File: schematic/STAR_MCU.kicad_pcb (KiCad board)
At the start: 2 copper layers, 39 parts, among them J1 HC-SR04, J11 6120XX21621_61200621621, J13 6120XX21621_61200821621, J14 6120XX21621_61200821621, J15 6120XX21621_61200821621, J16 6120XX21621_61200821621, J17 USB4216-03-A, J18 6120XX21621_61200621621, J19 6120XX21621_61200821621, J2 HC-SR04, J20 S5B-XH-A, J21 6120XX21621_61200621621, J3 HC-SR04, J4 HC-SR04, J5 HC-SR04, J6 HC-SR04, J8 Conn_02x20_Odd_Even, U1 DS18B20+, U2 ESP32-S3-WROOM-1-N16, U3 74HC139D,653, U4 SN74HC153DR, U5 RP2350_Stamp_XL

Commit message: Normalize KiCad symbol library structure
- Remove ul_ prefixes from Ultra Librarian exports (10 directories renamed, 2 duplicates deleted)
- Flatten directory structure (remove KiCad/KiCADv6 subdirectories from 93 components)
- Replace date-stamped filenames with part numbers (3 files renamed)
- Standardize separators: comma to hyphen (7 directories renamed)
- Update library table references (sym-lib-table: 84 entries, fp-lib-table: 85 entries)
- Update all schematic and PCB references (10 schematics + 10 PCBs)

Total changes:
- 100 component directories normalized to flat structure
- All library references updated and validated
- No ul_ prefixes, KiCad subdirs, date-stamped files, or commas in names remain
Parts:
- U3, U4: footprint 74HC139D,653:SOIC127P600X175-16N -> 74HC139D-653:SOIC127P600X175-16N
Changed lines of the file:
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@@
 		(embedded_fonts no)
 	)
-	(footprint "74HC139D,653:SOIC127P600X175-16N"
+	(footprint "74HC139D-653:SOIC127P600X175-16N"
 		(layer "F.Cu")
 		(at 152.18 123.2)
@@
 		)
 	)
-	(footprint "74HC139D,653:SOIC127P600X175-16N"
+	(footprint "74HC139D-653:SOIC127P600X175-16N"
 		(layer "F.Cu")
 		(at 143.63 123.2)

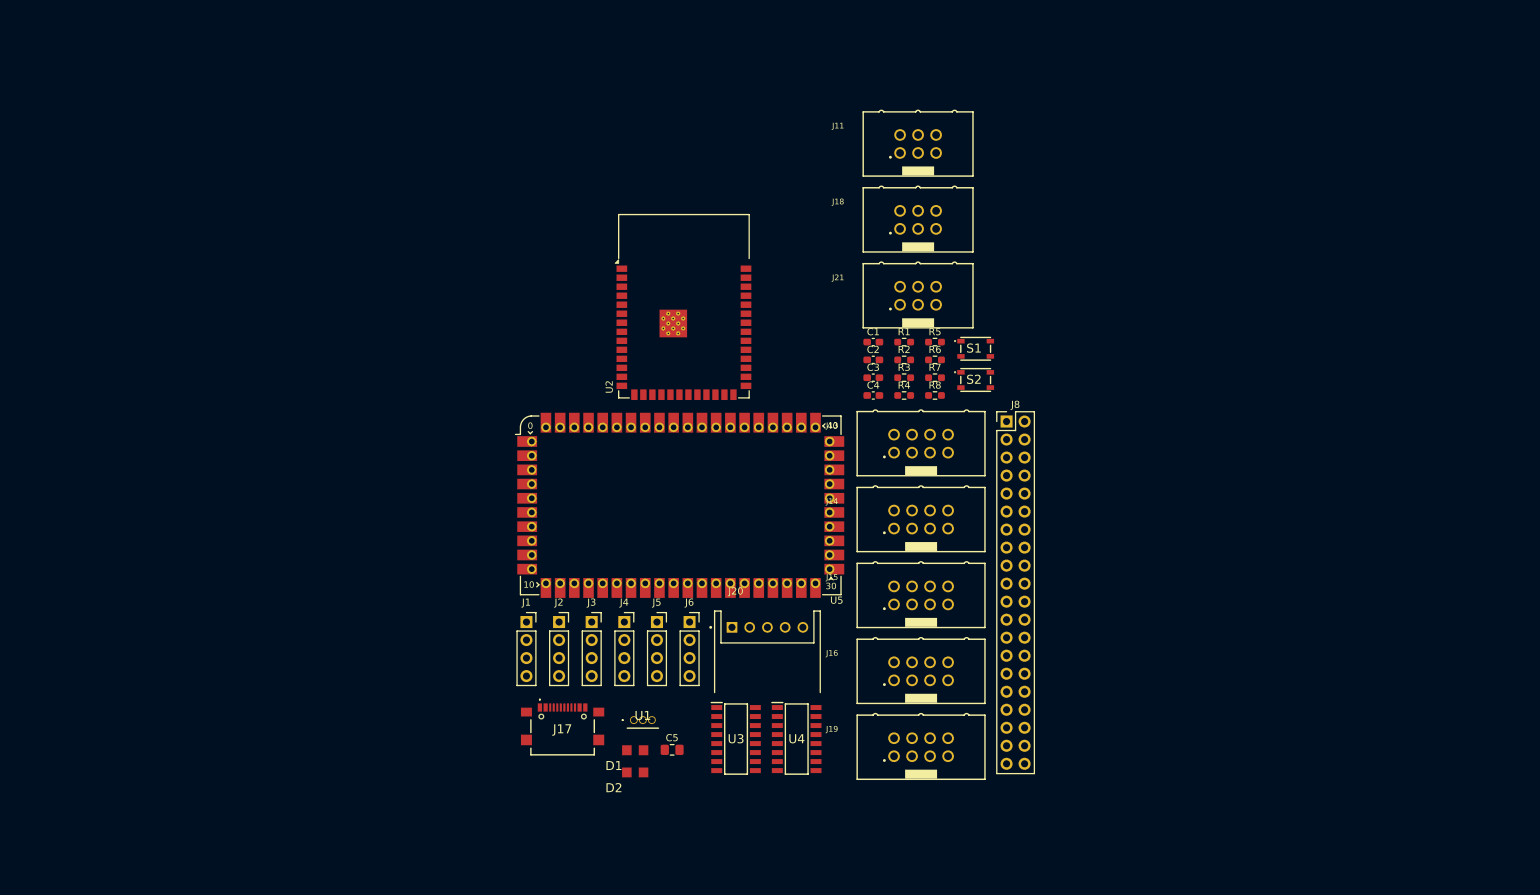
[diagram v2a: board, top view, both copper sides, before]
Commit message: fixed usb-c
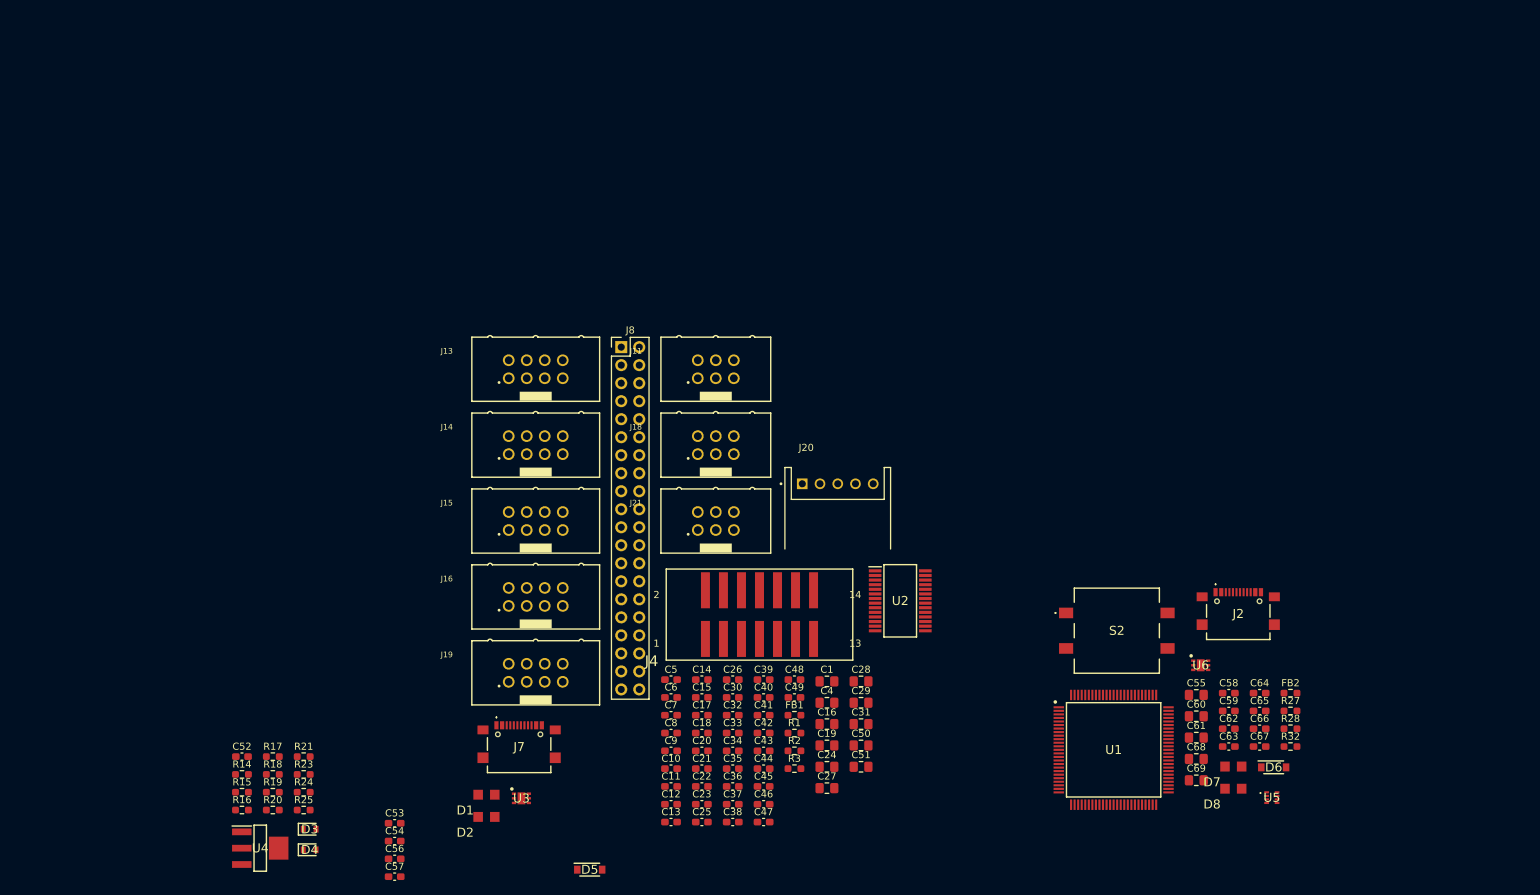
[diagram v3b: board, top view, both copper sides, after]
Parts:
- removed C2: 1u, Capacitor_SMD:C_0603_1608Metric_Pad1.08x0.95mm_HandSolder
- removed C3: 100n, Capacitor_SMD:C_0603_1608Metric_Pad1.08x0.95mm_HandSolder
- removed J1, J3, J5, J6: HC-SR04, Connector_PinSocket_2.54mm:PinSocket_1x04_P2.54mm_Vertical
- removed J17: USB4216-03-A, USB4216-03-A:USB421603A
- removed R4, R5, R8: 10k, Resistor_SMD:R_0603_1608Metric_Pad0.98x0.95mm_HandSolder
- removed R6, R7: 5k1, Resistor_SMD:R_0603_1608Metric_Pad0.98x0.95mm_HandSolder
- removed S1: ESP_RST, SKRPACE010:SMT_4.2X3.2_
- added C10: 1u, Capacitor_SMD:C_0603_1608Metric_Pad1.08x0.95mm_HandSolder, F.Cu at (134.5, 127.4)
- added C11: 1u, Capacitor_SMD:C_0603_1608Metric_Pad1.08x0.95mm_HandSolder, F.Cu at (134.5, 129.9)
- added C12: 1u, Capacitor_SMD:C_0603_1608Metric_Pad1.08x0.95mm_HandSolder, F.Cu at (134.5, 132.4)
- added C13: 1u, Capacitor_SMD:C_0603_1608Metric_Pad1.08x0.95mm_HandSolder, F.Cu at (134.5, 134.9)
- added C14: 1u, Capacitor_SMD:C_0603_1608Metric_Pad1.08x0.95mm_HandSolder, F.Cu at (138.8, 114.8)
- added C15: 220n, Capacitor_SMD:C_0603_1608Metric_Pad1.08x0.95mm_HandSolder, F.Cu at (138.8, 117.3)
- added C16: 10u, Capacitor_SMD:C_0805_2012Metric_Pad1.18x1.45mm_HandSolder, F.Cu at (156.4, 121.1)
- added C17: 100n, Capacitor_SMD:C_0603_1608Metric_Pad1.08x0.95mm_HandSolder, F.Cu at (138.8, 119.8)
- added C18: 10n, Capacitor_SMD:C_0603_1608Metric_Pad1.08x0.95mm_HandSolder, F.Cu at (138.8, 122.3)
- added C19: 10u, Capacitor_SMD:C_0805_2012Metric_Pad1.18x1.45mm_HandSolder, F.Cu at (156.4, 124.1)
- added C20: 100n, Capacitor_SMD:C_0603_1608Metric_Pad1.08x0.95mm_HandSolder, F.Cu at (138.8, 124.9)
- added C21: 1u, Capacitor_SMD:C_0603_1608Metric_Pad1.08x0.95mm_HandSolder, F.Cu at (138.8, 127.4)
- added C22: 1u, Capacitor_SMD:C_0603_1608Metric_Pad1.08x0.95mm_HandSolder, F.Cu at (138.8, 129.9)
- added C23: 10n, Capacitor_SMD:C_0603_1608Metric_Pad1.08x0.95mm_HandSolder, F.Cu at (138.8, 132.4)
- added C24: 10u, Capacitor_SMD:C_0805_2012Metric_Pad1.18x1.45mm_HandSolder, F.Cu at (156.4, 127.1)
- added C25: 100n, Capacitor_SMD:C_0603_1608Metric_Pad1.08x0.95mm_HandSolder, F.Cu at (138.8, 134.9)
- added C26: 10n, Capacitor_SMD:C_0603_1608Metric_Pad1.08x0.95mm_HandSolder, F.Cu at (143.2, 114.8)
- added C27: 10u, Capacitor_SMD:C_0805_2012Metric_Pad1.18x1.45mm_HandSolder, F.Cu at (156.4, 130.1)
- added C28: 10u, Capacitor_SMD:C_0805_2012Metric_Pad1.18x1.45mm_HandSolder, F.Cu at (161.3, 115.1)
- added C29: 10u, Capacitor_SMD:C_0805_2012Metric_Pad1.18x1.45mm_HandSolder, F.Cu at (161.3, 118.1)
- added C30: 100n, Capacitor_SMD:C_0603_1608Metric_Pad1.08x0.95mm_HandSolder, F.Cu at (143.2, 117.3)
- added C31: 10u, Capacitor_SMD:C_0805_2012Metric_Pad1.18x1.45mm_HandSolder, F.Cu at (161.3, 121.1)
- added C32: 10n, Capacitor_SMD:C_0603_1608Metric_Pad1.08x0.95mm_HandSolder, F.Cu at (143.2, 119.8)
- added C33: 100n, Capacitor_SMD:C_0603_1608Metric_Pad1.08x0.95mm_HandSolder, F.Cu at (143.2, 122.3)
- added C34: 100n, Capacitor_SMD:C_0603_1608Metric_Pad1.08x0.95mm_HandSolder, F.Cu at (143.2, 124.9)
- added C35: 100n, Capacitor_SMD:C_0603_1608Metric_Pad1.08x0.95mm_HandSolder, F.Cu at (143.2, 127.4)
- added C36: 100n, Capacitor_SMD:C_0603_1608Metric_Pad1.08x0.95mm_HandSolder, F.Cu at (143.2, 129.9)
- added C37: 100n, Capacitor_SMD:C_0603_1608Metric_Pad1.08x0.95mm_HandSolder, F.Cu at (143.2, 132.4)
- added C38: 100n, Capacitor_SMD:C_0603_1608Metric_Pad1.08x0.95mm_HandSolder, F.Cu at (143.2, 134.9)
- added C39: 100n, Capacitor_SMD:C_0603_1608Metric_Pad1.08x0.95mm_HandSolder, F.Cu at (147.5, 114.8)
- added C40: 100n, Capacitor_SMD:C_0603_1608Metric_Pad1.08x0.95mm_HandSolder, F.Cu at (147.5, 117.3)
- added C41: 100n, Capacitor_SMD:C_0603_1608Metric_Pad1.08x0.95mm_HandSolder, F.Cu at (147.5, 119.8)
- added C42: 100n, Capacitor_SMD:C_0603_1608Metric_Pad1.08x0.95mm_HandSolder, F.Cu at (147.5, 122.3)
- added C43: 1u, Capacitor_SMD:C_0603_1608Metric_Pad1.08x0.95mm_HandSolder, F.Cu at (147.5, 124.9)
- added C44: 100n, Capacitor_SMD:C_0603_1608Metric_Pad1.08x0.95mm_HandSolder, F.Cu at (147.5, 127.4)
- added C45: 10n, Capacitor_SMD:C_0603_1608Metric_Pad1.08x0.95mm_HandSolder, F.Cu at (147.5, 129.9)
- added C46: 10n, Capacitor_SMD:C_0603_1608Metric_Pad1.08x0.95mm_HandSolder, F.Cu at (147.5, 132.4)
- added C47: 10n, Capacitor_SMD:C_0603_1608Metric_Pad1.08x0.95mm_HandSolder, F.Cu at (147.5, 134.9)
- added C48: 10n, Capacitor_SMD:C_0603_1608Metric_Pad1.08x0.95mm_HandSolder, F.Cu at (151.9, 114.8)
- added C49: 100n, Capacitor_SMD:C_0603_1608Metric_Pad1.08x0.95mm_HandSolder, F.Cu at (151.9, 117.3)
- added C50: 4u7, Capacitor_SMD:C_0805_2012Metric_Pad1.18x1.45mm_HandSolder, F.Cu at (161.3, 124.1)
- added C51: 4u7, Capacitor_SMD:C_0805_2012Metric_Pad1.18x1.45mm_HandSolder, F.Cu at (161.3, 127.1)
- added C52: 1u, Capacitor_SMD:C_0603_1608Metric_Pad1.08x0.95mm_HandSolder, F.Cu at (74.0, 125.7)
- added C53: 1u, Capacitor_SMD:C_0603_1608Metric_Pad1.08x0.95mm_HandSolder, F.Cu at (95.5, 135.1)
- added C54: 100n, Capacitor_SMD:C_0603_1608Metric_Pad1.08x0.95mm_HandSolder, F.Cu at (95.5, 137.6)
- added C55: 4u7, Capacitor_SMD:C_0805_2012Metric_Pad1.18x1.45mm_HandSolder, F.Cu at (208.5, 117.0)
- added C56: 1u, Capacitor_SMD:C_0603_1608Metric_Pad1.08x0.95mm_HandSolder, F.Cu at (95.5, 140.1)
- added C57: 100n, Capacitor_SMD:C_0603_1608Metric_Pad1.08x0.95mm_HandSolder, F.Cu at (95.5, 142.6)
- added C58: 1u, Capacitor_SMD:C_0603_1608Metric_Pad1.08x0.95mm_HandSolder, F.Cu at (213.1, 116.7)
- added C59: 1u, Capacitor_SMD:C_0603_1608Metric_Pad1.08x0.95mm_HandSolder, F.Cu at (213.1, 119.2)
- added C6: 1u, Capacitor_SMD:C_0603_1608Metric_Pad1.08x0.95mm_HandSolder, F.Cu at (134.5, 117.3)
- added C60: 10u, Capacitor_SMD:C_0805_2012Metric_Pad1.18x1.45mm_HandSolder, F.Cu at (208.5, 120.0)
- added C61: 10u, Capacitor_SMD:C_0805_2012Metric_Pad1.18x1.45mm_HandSolder, F.Cu at (208.5, 123.0)
- added C62: 1u, Capacitor_SMD:C_0603_1608Metric_Pad1.08x0.95mm_HandSolder, F.Cu at (213.1, 121.7)
- added C63: 10n, Capacitor_SMD:C_0603_1608Metric_Pad1.08x0.95mm_HandSolder, F.Cu at (213.1, 124.3)
- added C64: 10n, Capacitor_SMD:C_0603_1608Metric_Pad1.08x0.95mm_HandSolder, F.Cu at (217.4, 116.7)
- added C65: 10n, Capacitor_SMD:C_0603_1608Metric_Pad1.08x0.95mm_HandSolder, F.Cu at (217.4, 119.2)
- added C66: 10n, Capacitor_SMD:C_0603_1608Metric_Pad1.08x0.95mm_HandSolder, F.Cu at (217.4, 121.7)
- added C67: 100n, Capacitor_SMD:C_0603_1608Metric_Pad1.08x0.95mm_HandSolder, F.Cu at (217.4, 124.3)
- added C68: 4u7, Capacitor_SMD:C_0805_2012Metric_Pad1.18x1.45mm_HandSolder, F.Cu at (208.5, 126.0)
- added C69: 4u7, Capacitor_SMD:C_0805_2012Metric_Pad1.18x1.45mm_HandSolder, F.Cu at (208.5, 129.0)
- added C7: 1u, Capacitor_SMD:C_0603_1608Metric_Pad1.08x0.95mm_HandSolder, F.Cu at (134.5, 119.8)
- added C8: 1u, Capacitor_SMD:C_0603_1608Metric_Pad1.08x0.95mm_HandSolder, F.Cu at (134.5, 122.3)
- added C9: 1u, Capacitor_SMD:C_0603_1608Metric_Pad1.08x0.95mm_HandSolder, F.Cu at (134.5, 124.9)
- added D3: RED, SML-D12Y1WT86:LEDC1608X55N, F.Cu at (83.5, 135.9)
- added D4: RED, SML-D12Y1WT86:LEDC1608X55N, F.Cu at (83.5, 138.8)
- added D5: 1N4007W-T, 1N4007W-T:SODFL3818X130N, F.Cu at (123.0, 141.6)
- added D6: 1N4007W-T, 1N4007W-T:SODFL3818X130N, F.Cu at (219.4, 127.2)
- added D7: 82306050029, 82306050029:WESURGE_0603134, F.Cu at (213.7, 127.1)
- added D8: 82306050029, 82306050029:WESURGE_0603134, F.Cu at (213.7, 130.2)
- added FB1: 22R, Resistor_SMD:R_0603_1608Metric_Pad0.98x0.95mm_HandSolder, F.Cu at (151.9, 119.8)
- added FB2: 22R, Resistor_SMD:R_0603_1608Metric_Pad0.98x0.95mm_HandSolder, F.Cu at (221.8, 116.7)
- added J7: USB4216-03-A, USB4216-03-A:USB421603A, F.Cu at (113.0, 124.6)
- added R14: 1k, Resistor_SMD:R_0603_1608Metric_Pad0.98x0.95mm_HandSolder, F.Cu at (74.0, 128.2)
- added R15: 1k, Resistor_SMD:R_0603_1608Metric_Pad0.98x0.95mm_HandSolder, F.Cu at (74.0, 130.7)
- added R16: 10k, Resistor_SMD:R_0603_1608Metric_Pad0.98x0.95mm_HandSolder, F.Cu at (74.0, 133.2)
- added R17: 10k, Resistor_SMD:R_0603_1608Metric_Pad0.98x0.95mm_HandSolder, F.Cu at (78.3, 125.7)
- added R18: 10k, Resistor_SMD:R_0603_1608Metric_Pad0.98x0.95mm_HandSolder, F.Cu at (78.3, 128.2)
- added R19: 10k, Resistor_SMD:R_0603_1608Metric_Pad0.98x0.95mm_HandSolder, F.Cu at (78.3, 130.7)
- added R20: 10k, Resistor_SMD:R_0603_1608Metric_Pad0.98x0.95mm_HandSolder, F.Cu at (78.3, 133.2)
- added R21: 10k, Resistor_SMD:R_0603_1608Metric_Pad0.98x0.95mm_HandSolder, F.Cu at (82.7, 125.7)
- added R23: 10k, Resistor_SMD:R_0603_1608Metric_Pad0.98x0.95mm_HandSolder, F.Cu at (82.7, 128.2)
- added R24: 10k, Resistor_SMD:R_0603_1608Metric_Pad0.98x0.95mm_HandSolder, F.Cu at (82.7, 130.7)
- added R25: 10k, Resistor_SMD:R_0603_1608Metric_Pad0.98x0.95mm_HandSolder, F.Cu at (82.7, 133.2)
- added R27: 10k, Resistor_SMD:R_0603_1608Metric_Pad0.98x0.95mm_HandSolder, F.Cu at (221.8, 119.2)
- added R28: 10k, Resistor_SMD:R_0603_1608Metric_Pad0.98x0.95mm_HandSolder, F.Cu at (221.8, 121.7)
- added R32: 15k, Resistor_SMD:R_0603_1608Metric_Pad0.98x0.95mm_HandSolder, F.Cu at (221.8, 124.3)
- added U6: TVS2200DRV, TVS2200DRVR:SON65P200X200X80-7N, F.Cu at (209.1, 112.8)
- C1, C4: value 100n -> 10u; footprint Capacitor_SMD:C_0603_1608Metric_Pad1.08x0.95mm_HandSolder -> Capacitor_SMD:C_0805_2012Metric_Pad1.18x1.45mm_HandSolder
- C5: value 10u -> 100n; footprint Capacitor_SMD:C_0805_2012Metric_Pad1.18x1.45mm_HandSolder -> Capacitor_SMD:C_0603_1608Metric_Pad1.08x0.95mm_HandSolder
- J2: value HC-SR04 -> USB4216-03-A; footprint Connector_PinSocket_2.54mm:PinSocket_1x04_P2.54mm_Vertical -> USB4216-03-A:USB421603A
- J4: value HC-SR04 -> E1E2-Emulator-Interface; footprint Connector_PinSocket_2.54mm:PinSocket_1x04_P2.54mm_Vertical -> E1E2-Emulator-Interface:SAMTEC-HTST-107-01-X-DV
- S2: value ESP_BOOT -> PTS125SM73SMTR21M_LFS; footprint SKRPACE010:SMT_4.2X3.2_ -> PTS125SM73SMTR21M_LFS:PTS125SM73SMTR21MLFS
- U1: value DS18B20+ -> R5F572NNHGFP-30; footprint DS18B20+:DS18B20 -> R5F572NNHGFP-30:QFP50P1600X1600X170-100N
- U2: value ESP32-S3-WROOM-1-N16 -> CY7C65213A-28PVXI; footprint RF_Module:ESP32-S3-WROOM-1 -> CY7C65213A-28PVXI:SOP65P780X200-28N
- U3: value 74HC139D,653 -> TVS2200DRV; footprint 74HC139D-653:SOIC127P600X175-16N -> TVS2200DRVR:SON65P200X200X80-7N
- U4: value SN74HC153DR -> LDL1117S33R; footprint 74HC139D-653:SOIC127P600X175-16N -> LDL1117S33R:SOT230P700X180-4N
- U5: value RP2350_Stamp_XL -> TPS2116DRLR; footprint rp2xxx:RP2xxx_Stamp_XL_THT -> TPS2116DRLR:TPS62932DRLR
- moved J2 95.8 mm to (214.4, 105.8)
- moved U5 93.0 mm to (219.2, 131.5)
- moved U4 77.2 mm to (76.5, 138.6)
- moved U1 66.5 mm to (196.9, 124.7)
- moved R2 57.2 mm to (151.9, 124.9)
- moved R3 57.2 mm to (151.9, 127.4)
- moved R1 57.2 mm to (151.9, 122.3)
- moved J8 55.3 mm to (127.4, 67.9)
- moved J13 55.3 mm to (115.4, 71.1)
- moved J14 55.3 mm to (115.4, 81.8)
- moved J15 55.3 mm to (115.4, 92.5)
- moved J16 55.3 mm to (115.4, 103.2)
- moved J19 55.3 mm to (115.4, 113.9)
- moved U2 51.5 mm to (166.8, 103.7)
- moved C1 48.3 mm to (156.4, 115.1)
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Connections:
- C1 pad 1: GND -> /BOARD_3V3
- C1 pad 2: Net-(C1-Pad2) -> GND
- C4 pad 1: GND -> /BOARD_3V3
- C4 pad 2: /MOTOR_DRIVER_P3V3 -> AVSS0-1
- C5 pad 1: /MOTOR_DRIVER_P3V3 -> /BOARD_3V3
- D1 pad 1: /USB_C_P -> /SCI_USBC_USBDP
- D2 pad 1: /USB_C_N -> /SCI_USBC_USBDN
- J4 pad 1: /MOTOR_DRIVER_P3V3 -> /EMU_TCK
- J4 pad 2: /HCSR04_TRIG4 -> GND
- J4 pad 3: /HCSR04_ECHO4 -> /EMU_TRSTn
- J4 pad 4: GND -> /EMU_EMLE
- J8 pad 11: /HCSR04_ECHO1 -> unconnected-(J8-Pin_11-Pad11)
- J8 pad 12: /HCSR04_TRIG4 -> unconnected-(J8-Pin_12-Pad12)
- J8 pad 13: /HCSR04_TRIG2 -> unconnected-(J8-Pin_13-Pad13)
- J8 pad 15: /HCSR04_ECHO2 -> unconnected-(J8-Pin_15-Pad15)
- J8 pad 22: /HCSR04_ECHO4 -> unconnected-(J8-Pin_22-Pad22)
- J8 pad 26: /HCSR04_TRIG5 -> unconnected-(J8-Pin_26-Pad26)
- J8 pad 27: /MOTOR_DRIVER_MOTOR4_nFAULT -> unconnected-(J8-Pin_27-Pad27)
- J8 pad 28: /HCSR04_ECHO5 -> unconnected-(J8-Pin_28-Pad28)
- J8 pad 29: /MOTOR_DRIVER_MOTOR3_nFAULT -> unconnected-(J8-Pin_29-Pad29)
- J8 pad 31: /MOTOR_DRIVER_MOTOR2_nFAULT -> unconnected-(J8-Pin_31-Pad31)
- J8 pad 32: /HCSR04_TRIG6 -> unconnected-(J8-Pin_32-Pad32)
- J8 pad 33: /MOTOR_DRIVER_MOTOR1_nFAULT -> unconnected-(J8-Pin_33-Pad33)
- J8 pad 35: /HCSR04_TRIG3 -> unconnected-(J8-Pin_35-Pad35)
- J8 pad 36: /HCSR04_ECHO6 -> unconnected-(J8-Pin_36-Pad36)
- J8 pad 37: /HCSR04_ECHO3 -> unconnected-(J8-Pin_37-Pad37)
- J8 pad 7: /HCSR04_TRIG1 -> unconnected-(J8-Pin_7-Pad7)
- R3 pad 1: Net-(C1-Pad2) -> Net-(U1-XCIN)
- R3 pad 2: /MOTOR_DRIVER_P3V3 -> GND
- U1 pad 1: GND -> /BOARD_3V3
- U1 pad 2: /TEMPERATURE_SENSOR -> /EMU_EMLE
- U1 pad 3: /MOTOR_DRIVER_P3V3 -> AVSS0-1
- U2 pad 1: GND -> /SCI9_RXD1
- U2 pad 10: /MOTOR_DRIVER_MOTOR3_PH_IN2 -> Net-(U2-DCD#)
- U2 pad 11: /MOTOR_DRIVER_MOTOR4_EN_IN1 -> Net-(U2-CTS#)
- U2 pad 12: /FUEL_GUAGE_SMBD_SDA -> unconnected-(U2-GPIO4-Pad12)
- U2 pad 13: /USB_C_N -> Net-(U2-GPIO2)
- U2 pad 14: /USB_C_P -> unconnected-(U2-GPIO3-Pad14)
- U2 pad 15: unconnected-(U2-IO3-Pad15) -> /SCI_USBC_USBDP
- U2 pad 16: unconnected-(U2-IO46-Pad16) -> /SCI_USBC_USBDN
- U2 pad 17: /FUEL_GUAGE_SMBC_SCL -> Net-(U2-VCCD)
- U2 pad 18: /ESP_PI_SPI3_PM_CS -> GND
- U2 pad 19: /ESP_PI_SPI3_PM_COPI -> Net-(U2-RESET#)
- U2 pad 2: /MOTOR_DRIVER_P3V3 -> unconnected-(U2-DTR#-Pad2)
- U2 pad 20: /ESP_PI_SPI3_PM_SCLK -> /SCI_USBC_5V0
- U2 pad 21: /ESP_PI_SPI3_PM_CIPO -> GND
- U2 pad 22: /MOTOR_DRIVER_MOTOR2_EN_IN1 -> Net-(U2-GPIO1)
- U2 pad 23: /MOTOR_DRIVER_MOTOR4_PH_IN2 -> Net-(U2-GPIO0)
- U2 pad 24: /MOTOR_ENCODER_OUT1 -> unconnected-(U2-NC_1-Pad24)
- U2 pad 25: /TEMPERATURE_SENSOR -> unconnected-(U2-NC_2-Pad25)
- U2 pad 28: /MOTOR_DRIVER_SPI2_CM_COPI -> Net-(U2-GPIO7)
- U2 pad 3: Net-(U2-EN) -> unconnected-(U2-RTS#-Pad3)
- U2 pad 4: /MOTOR_DRIVER_MOTOR3_IPROPI -> /BOARD_3V3
- U2 pad 5: /MOTOR_DRIVER_MOTOR4_IPROPI -> /SCI9_TXD9
- U2 pad 6: /MOTOR_DRIVER_MOTOR1_EN_IN1 -> Net-(U2-RI#)
- U2 pad 7: /MOTOR_DRIVER_MOTOR1_PH_IN2 -> GND
- U2 pad 8: /MOTOR_DRIVER_MOTOR2_PH_IN2 -> Net-(U2-GPIO5)
- U2 pad 9: /MOTOR_DRIVER_MOTOR3_EN_IN1 -> Net-(U2-DSR#)
- U3 pad 2: Net-(U2-IO38) -> GND
- U3 pad 3: Net-(U2-IO39) -> GND
- U3 pad 4: /MOTOR_DRIVER_SPI2_MOTOR1_nCS -> Net-(J7-VBUS_1)
- U3 pad 5: /MOTOR_DRIVER_SPI2_MOTOR2_nCS -> Net-(J7-VBUS_1)
- U3 pad 6: /MOTOR_DRIVER_SPI2_MOTOR3_nCS -> Net-(J7-VBUS_1)
- U3 pad 7: /MOTOR_DRIVER_SPI2_MOTOR4_nCS -> GND
- U4 pad 2: /MOTOR_ENCODER_SEL1 -> /BUS_3V3
- U4 pad 3: /MOTOR_DRIVER_ENCODER4_OUTPUT_A -> Net-(D5-K)
- U4 pad 4: /MOTOR_DRIVER_ENCODER3_OUTPUT_A -> /BUS_3V3
- U5 pad 1: unconnected-(U5A-GPIO0-Pad1) -> GND
- U5 pad 2: unconnected-(U5A-GPIO1-Pad2) -> /BOARD_3V3
- U5 pad 3: unconnected-(U5A-GPIO2-Pad3) -> /BUS_3V3
- U5 pad 4: unconnected-(U5A-GPIO3-Pad4) -> Net-(U5-PR1)
- U5 pad 5: unconnected-(U5A-GPIO4-Pad5) -> /BUS_3V3
- U5 pad 6: unconnected-(U5A-GPIO5-Pad6) -> /MOTOR_DRIVER_P3V3
- U5 pad 7: unconnected-(U5A-GPIO6-Pad7) -> /BOARD_3V3
